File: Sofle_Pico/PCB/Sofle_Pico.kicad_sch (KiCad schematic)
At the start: 77 parts, among them J1 Pimaroni Trackball, J2 4PIN, J3 OLED, J5 Conn_01x05_Socket, J6 Conn_01x05_Socket, SW1 SW_PUSH_LED, SW10 SW_PUSH_LED, SW11 SW_PUSH_LED, SW12 SW_PUSH_LED, SW13 SW_PUSH_LED, SW14 SW_PUSH_LED, SW15 SW_PUSH_LED, SW16 SW_PUSH_LED, SW17 SW_PUSH_LED, SW18 SW_PUSH_LED, SW19 SW_PUSH_LED, SW2 SW_PUSH_LED, SW20 SW_PUSH_LED, SW21 SW_PUSH_LED, SW22 SW_PUSH_LED, SW23 SW_PUSH_LED, SW24 SW_PUSH_LED, SW25 Rotary_Encoder_Switch, SW26 SW_PUSH_LED, SW27 SW_PUSH_LED, SW28 SW_PUSH_LED, SW29 SW_PUSH_LED, SW3 SW_PUSH_LED, SW30 SW_PUSH_LED, SW4 SW_PUSH_LED, SW5 SW_PUSH_LED, SW6 SW_PUSH_LED, SW7 SW_PUSH_LED, SW8 SW_PUSH_LED, SW9 SW_PUSH_LED, U1 SN74AHCT1G125, U3 Pico

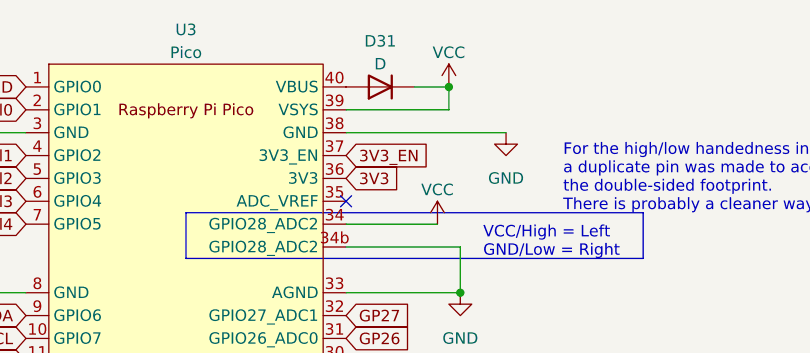
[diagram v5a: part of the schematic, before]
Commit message: Refactored power circuit to remove extra diode sent this version out for production at JLC
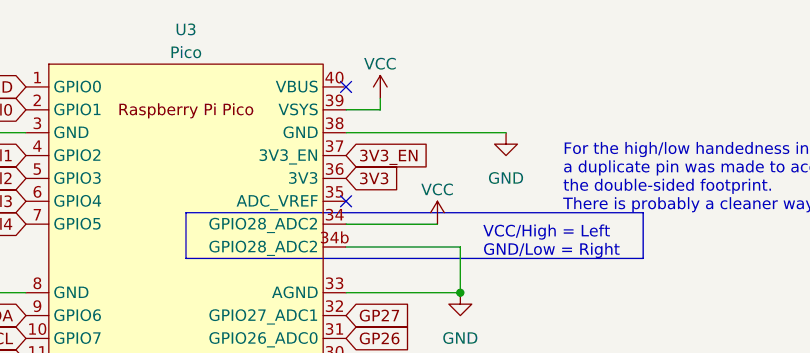
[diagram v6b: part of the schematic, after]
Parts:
- removed D31: D, Sofle_Pico:D_SOD-123_DO-35_Hybrid_DoubleSided_V2, symbol Device:D
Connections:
- no-connect marks 8 -> 9
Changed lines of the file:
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@@
   (junction (at 172.72 25.4) (diameter 0) (color 0 0 0 0)
   )
-  (junction (at 73.66 21.59) (diameter 0) (color 0 0 0 0)
-  )
   (junction (at 158.75 97.79) (diameter 0) (color 0 0 0 0)
   )
@@
   (no_connect (at 44.45 80.01))
   (no_connect (at 41.91 80.01))
+  (no_connect (at 62.23 21.59))
   (no_connect (at 62.23 34.29))
   (no_connect (at 69.85 162.56))
@@
     (stroke (width 0) (type default))
   )
-  (wire (pts (xy 69.85 21.59) (xy 73.66 21.59))
-    (stroke (width 0) (type default))
-  )
   (wire (pts (xy 221.615 56.515) (xy 221.615 53.34))
     (stroke (width 0) (type default))
@@
     (stroke (width 0) (type default))
   )
+  (wire (pts (xy 66.04 22.86) (xy 66.04 24.13))
+    (stroke (width 0) (type default))
+  )
   (wire (pts (xy 199.39 147.32) (xy 219.71 147.32))
     (stroke (width 0) (type default))
@@
     (stroke (width 0) (type default))
   )
-  (wire (pts (xy 73.66 24.13) (xy 73.66 21.59))
-    (stroke (width 0) (type default))
-  )
   (wire (pts (xy 236.855 45.085) (xy 236.855 48.26))
     (stroke (width 0) (type default))
@@
     (stroke (width 0) (type default))
   )
-  (wire (pts (xy 62.23 24.13) (xy 73.66 24.13))
+  (wire (pts (xy 62.23 24.13) (xy 66.04 24.13))
     (stroke (width 0) (type default))
   )
@@
     )
   )
-  (symbol (lib_id "power:VCC") (at 73.66 21.59 0) (unit 1)
+  (symbol (lib_id "power:VCC") (at 66.04 22.86 0) (unit 1)
     (in_bom yes) (on_board yes) (dnp no) (fields_autoplaced)
-    (property "Reference" "#PWR06" (at 73.66 25.4 0)
+    (property "Reference" "#PWR06" (at 66.04 26.67 0)
       (effects (font (size 1.27 1.27)) hide)
     )
-    (property "Value" "VCC" (at 73.66 17.78 0)
+    (property "Value" "VCC" (at 66.04 19.05 0)
       (effects (font (size 1.27 1.27)))
     )
-    (property "Footprint" "" (at 73.66 21.59 0)
+    (property "Footprint" "" (at 66.04 22.86 0)
       (effects (font (size 1.27 1.27)) hide)
     )
-    (property "Datasheet" "" (at 73.66 21.59 0)
+    (property "Datasheet" "" (at 66.04 22.86 0)
       (effects (font (size 1.27 1.27)) hide)
     )
@@
         )
       )
-    )
-  )
-  (symbol (lib_id "Device:D") (at 66.04 21.59 180) (unit 1)
-    (in_bom yes) (on_board yes) (dnp no) (fields_autoplaced)
-    (property "Reference" "D31" (at 66.04 16.51 0)
-      (effects (font (size 1.27 1.27)))
-    )
-    (property "Value" "D" (at 66.04 19.05 0)
-      (effects (font (size 1.27 1.27)))
-    )
-    (property "Footprint" "Sofle_Pico:D_SOD-123_DO-35_Hybrid_DoubleSided_V2" (at 66.04 21.59 0)
-      (effects (font (size 1.27 1.27)) hide)
-    )
-    (property "Datasheet" "~" (at 66.04 21.59 0)
-      (effects (font (size 1.27 1.27)) hide)
-    )
-    (property "Sim.Device" "D" (at 66.04 21.59 0)
-      (effects (font (size 1.27 1.27)) hide)
-    )
-    (property "Sim.Pins" "1=K 2=A" (at 66.04 21.59 0)
-      (effects (font (size 1.27 1.27)) hide)
-    )
-    (pin "1")
-    (pin "2")
-    (instances
-      (project "Sofle_Pico"
-        (path "/06057b3a-55ab-4f4e-913e-2aeec5ff3587"
-          (reference "D31") (unit 1)
-        )
-      )
-      (project "Sofle_v3"
-        (path "/aae4773e-62e9-4e6e-acb6-89e78a092249"
-          (reference "D31") (unit 1)
-        )
-      )

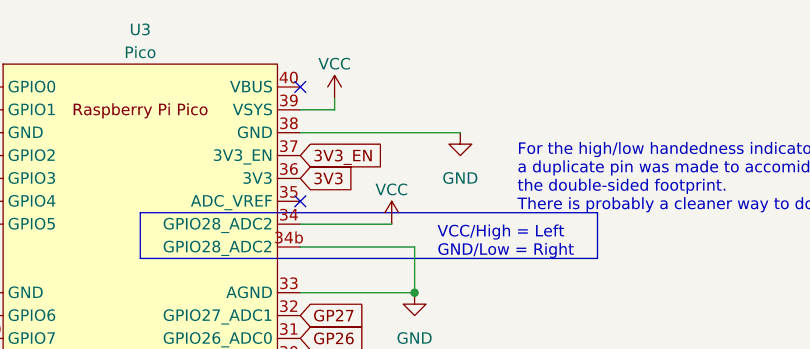
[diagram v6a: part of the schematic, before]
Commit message: Refactored power circuit to include Schottky diode
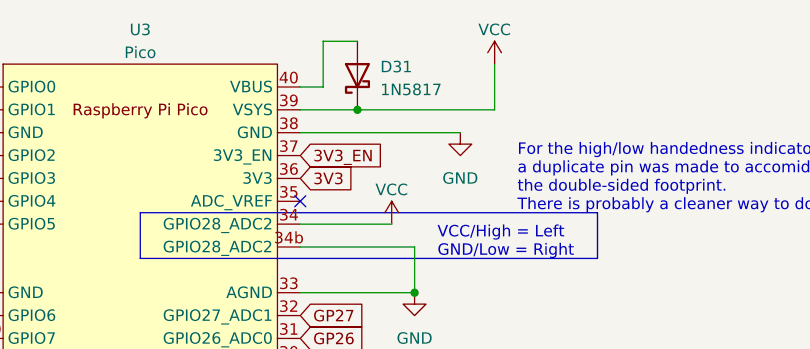
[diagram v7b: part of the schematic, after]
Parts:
- added D31: 1N5817, Sofle_Pico:D_DO-41_SOD81_P10.16mm_Horizontal, symbol Diode:1N5817
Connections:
- net VCC: now also D31.1 (K)
- net at U3.40 (VBUS): now also D31.2 (A)
- no-connect marks 9 -> 8
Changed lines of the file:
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@@
   (junction (at 158.75 97.79) (diameter 0) (color 0 0 0 0)
   )
+  (junction (at 68.58 24.13) (diameter 0) (color 0 0 0 0)
+  )
   (junction (at 240.03 163.83) (diameter 0) (color 0 0 0 0)
   )
@@
   (no_connect (at 44.45 80.01))
   (no_connect (at 41.91 80.01))
-  (no_connect (at 62.23 21.59))
   (no_connect (at 62.23 34.29))
   (no_connect (at 69.85 162.56))
@@
     (stroke (width 0) (type default))
   )
-  (wire (pts (xy 66.04 22.86) (xy 66.04 24.13))
+  (wire (pts (xy 83.82 19.05) (xy 83.82 24.13))
     (stroke (width 0) (type default))
   )
@@
     (stroke (width 0) (type default))
   )
+  (wire (pts (xy 62.23 21.59) (xy 64.77 21.59))
+    (stroke (width 0) (type default))
+  )
   (wire (pts (xy 204.47 123.19) (xy 204.47 139.7))
     (stroke (width 0) (type default))
   )
+  (wire (pts (xy 64.77 16.51) (xy 68.58 16.51))
+    (stroke (width 0) (type default))
+  )
   (wire (pts (xy 29.21 104.14) (xy 24.13 104.14))
     (stroke (width 0) (type default))
@@
     (stroke (width 0) (type default))
   )
+  (wire (pts (xy 68.58 24.13) (xy 83.82 24.13))
+    (stroke (width 0) (type default))
+  )
   (wire (pts (xy 216.535 41.91) (xy 216.535 45.085))
     (stroke (width 0) (type default))
@@
     (stroke (width 0) (type default))
   )
+  (wire (pts (xy 64.77 21.59) (xy 64.77 16.51))
+    (stroke (width 0) (type default))
+  )
   (wire (pts (xy 240.03 130.81) (xy 260.35 130.81))
     (stroke (width 0) (type default))
@@
     (stroke (width 0) (type default))
   )
-  (wire (pts (xy 62.23 24.13) (xy 66.04 24.13))
+  (wire (pts (xy 62.23 24.13) (xy 68.58 24.13))
     (stroke (width 0) (type default))
   )
@@
     )
   )
+  (symbol (lib_id "Diode:1N5817") (at 68.58 20.32 90) (unit 1)
+    (in_bom yes) (on_board yes) (dnp no) (fields_autoplaced)
+    (property "Reference" "D31" (at 71.12 19.3675 90)
+      (effects (font (size 1.27 1.27)) (justify right))
+    )
+    (property "Value" "1N5817" (at 71.12 21.9075 90)
+      (effects (font (size 1.27 1.27)) (justify right))
+    )
+    (property "Footprint" "Sofle_Pico:D_DO-41_SOD81_P10.16mm_Horizontal" (at 73.025 20.32 0)
+      (effects (font (size 1.27 1.27)) hide)
+    )
+    (property "Datasheet" "http://www.vishay.com/docs/88525/1n5817.pdf" (at 68.58 20.32 0)
+      (effects (font (size 1.27 1.27)) hide)
+    )
+    (pin "1")
+    (pin "2")
+    (instances
+      (project "Sofle_Pico"
+        (path "/06057b3a-55ab-4f4e-913e-2aeec5ff3587"
+          (reference "D31") (unit 1)
+        )
+      )
+    )
+  )
   (symbol (lib_id "power:GND") (at 16.51 69.85 0) (unit 1)
     (in_bom yes) (on_board yes) (dnp no) (fields_autoplaced)
@@
     )
   )
-  (symbol (lib_id "power:VCC") (at 66.04 22.86 0) (unit 1)
+  (symbol (lib_id "power:VCC") (at 83.82 19.05 0) (unit 1)
     (in_bom yes) (on_board yes) (dnp no) (fields_autoplaced)
-    (property "Reference" "#PWR06" (at 66.04 26.67 0)
+    (property "Reference" "#PWR06" (at 83.82 22.86 0)
       (effects (font (size 1.27 1.27)) hide)
     )
-    (property "Value" "VCC" (at 66.04 19.05 0)
+    (property "Value" "VCC" (at 83.82 15.24 0)
       (effects (font (size 1.27 1.27)))
     )
-    (property "Footprint" "" (at 66.04 22.86 0)
+    (property "Footprint" "" (at 83.82 19.05 0)
       (effects (font (size 1.27 1.27)) hide)
     )
-    (property "Datasheet" "" (at 66.04 22.86 0)
+    (property "Datasheet" "" (at 83.82 19.05 0)
       (effects (font (size 1.27 1.27)) hide)
     )

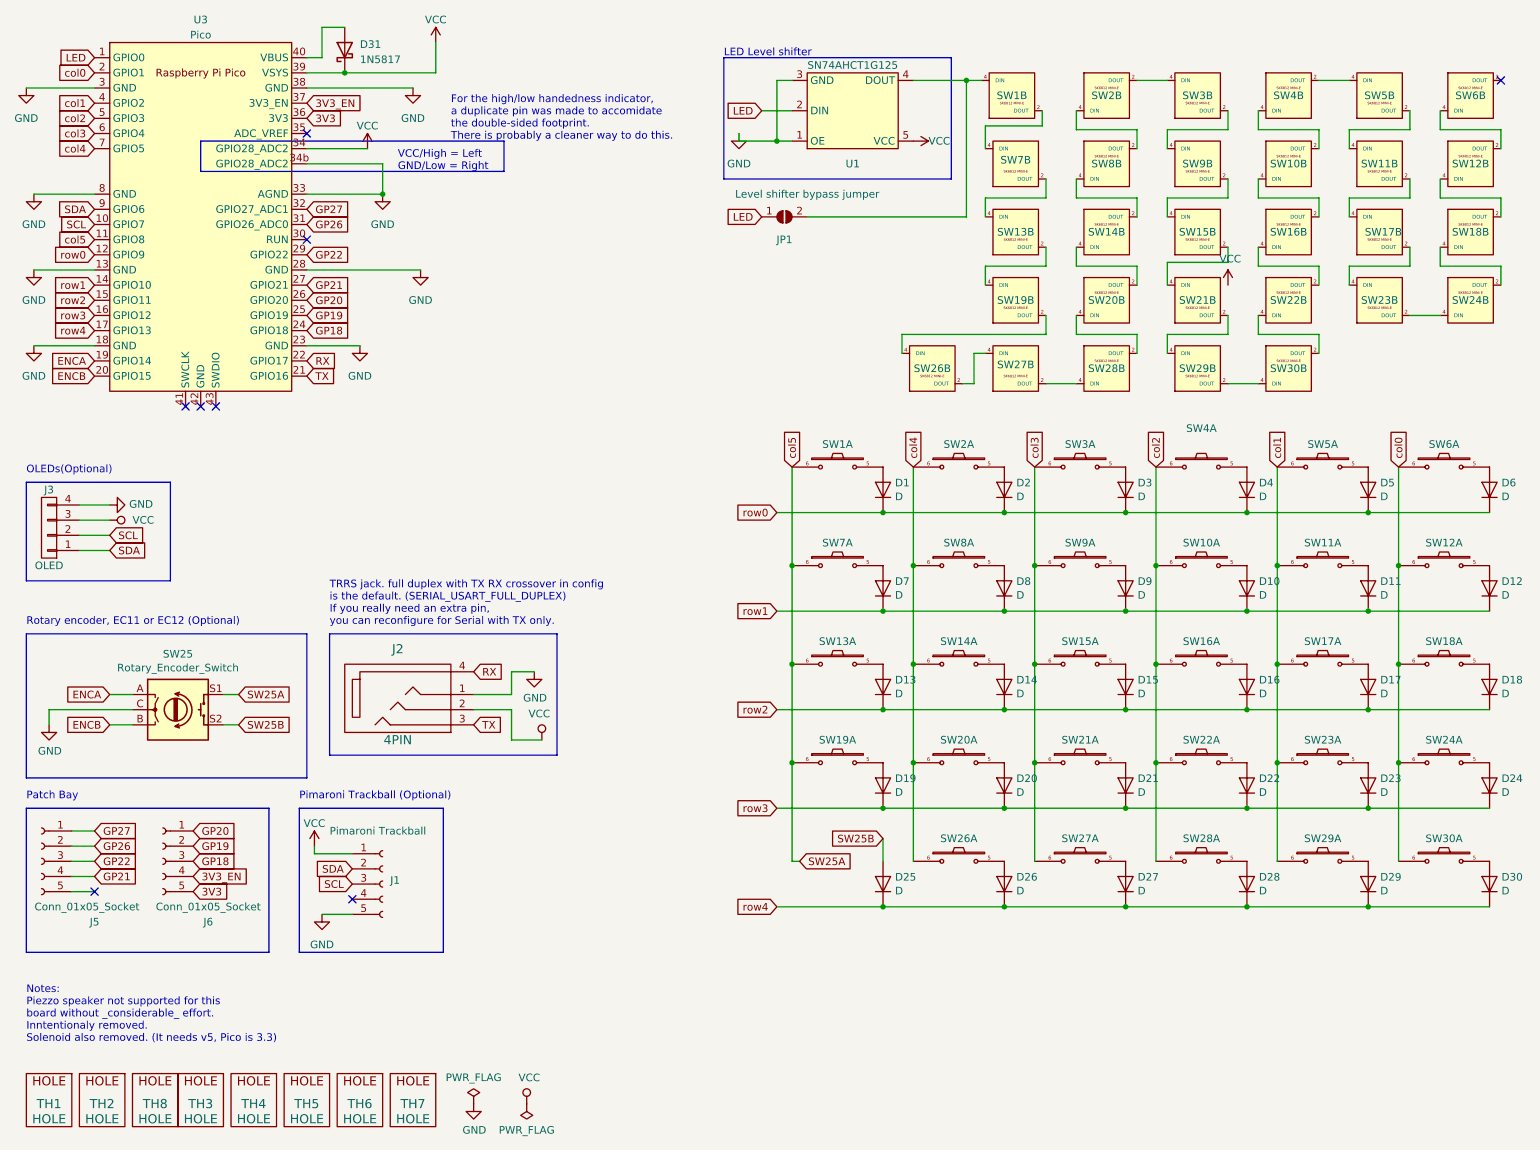
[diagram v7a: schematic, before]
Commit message: Moved handedness pin from GP28 to GP18 to support WeAct clones
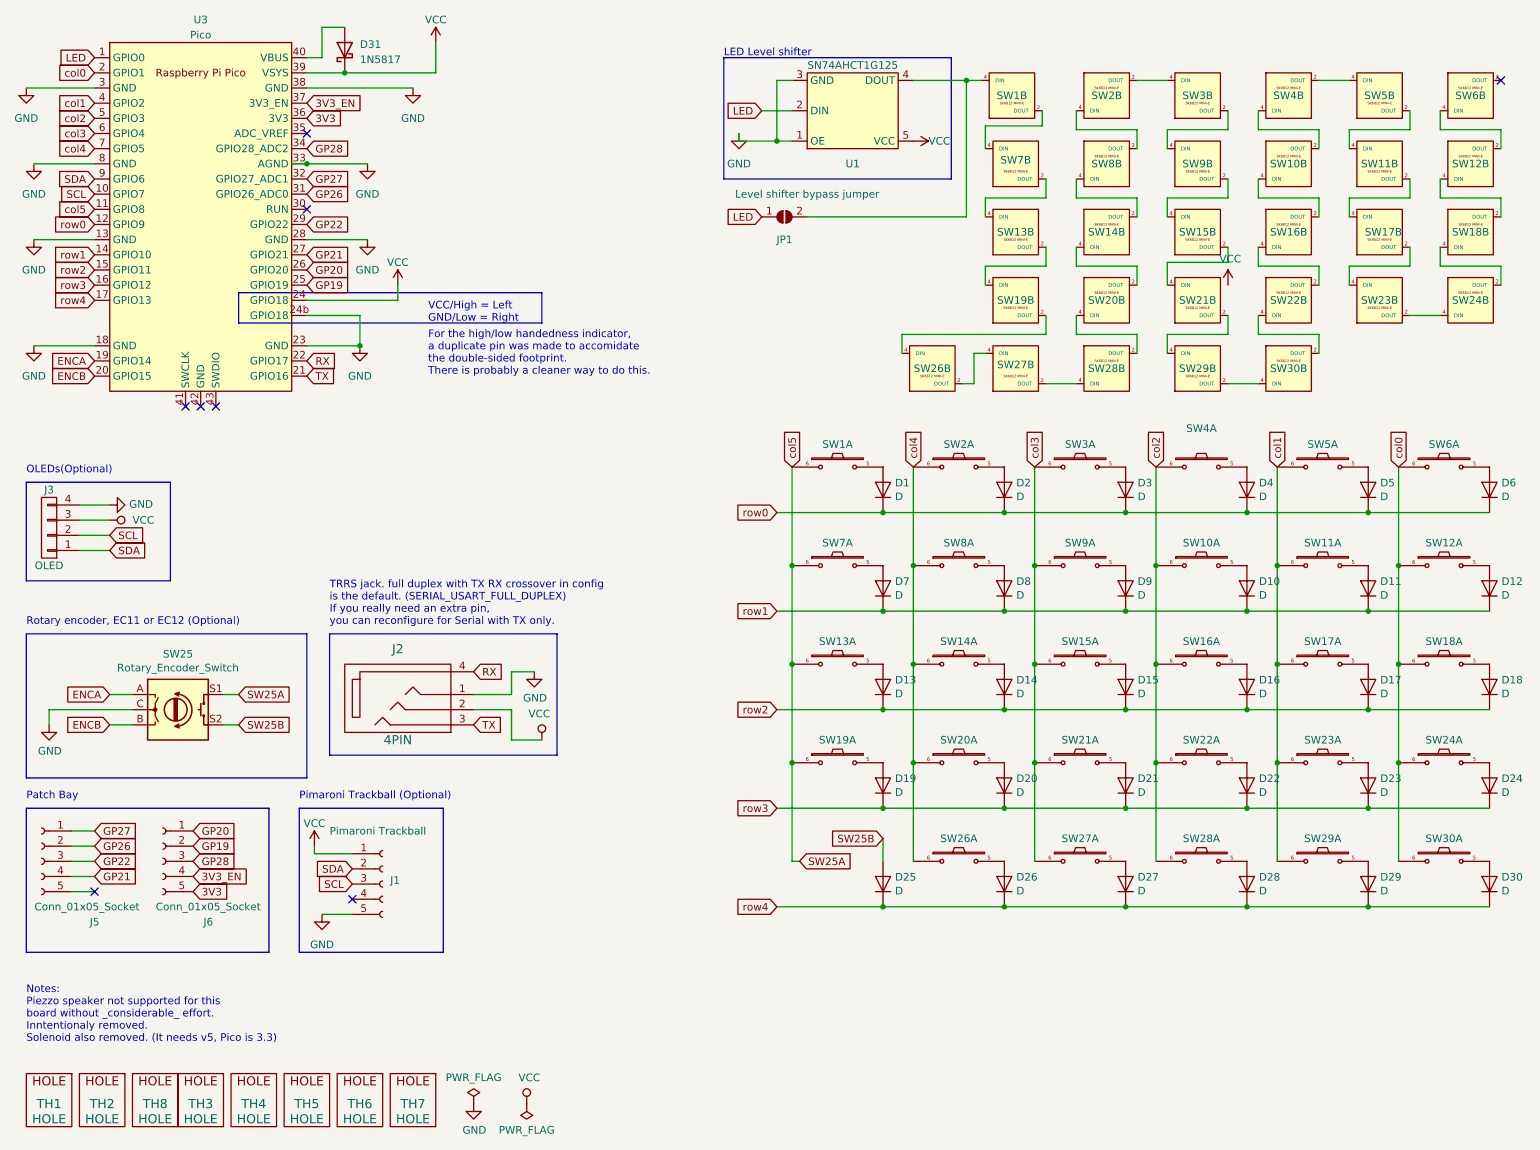
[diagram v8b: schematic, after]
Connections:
- net GND: now also U3.24b (GPIO18); no longer U3.34b (GPIO28_ADC2)
- net VCC: now also U3.24 (GPIO18); no longer U3.34 (GPIO28_ADC2)
- net GP18 renamed GP28
- net GP28: now also U3.34 (GPIO28_ADC2); no longer U3.24 (GPIO18)
